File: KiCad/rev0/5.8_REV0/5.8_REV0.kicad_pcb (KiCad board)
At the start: 4 copper layers, 36 x 14.5 mm, 9 parts, among them J1 Conn_Coaxial, J2 Conn_01x02, U1 PMA3-83LN+

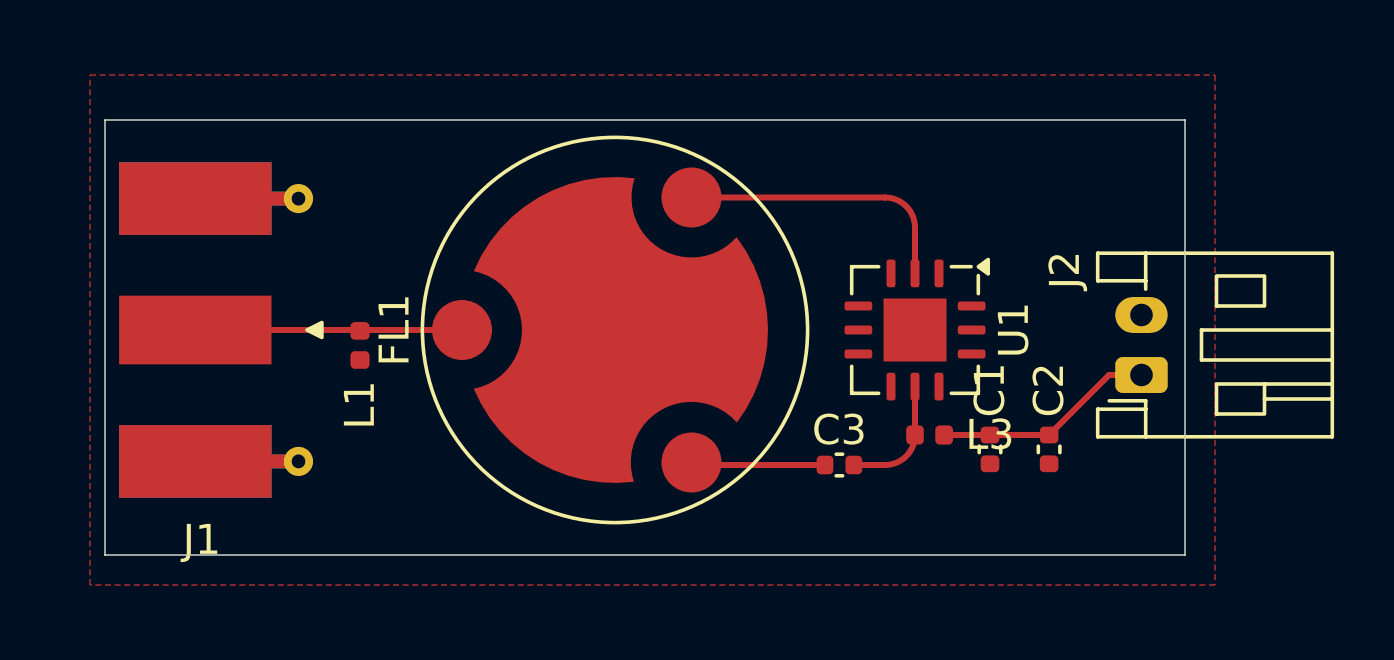
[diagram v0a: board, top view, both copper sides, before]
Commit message: Added sims and changed to microstrips
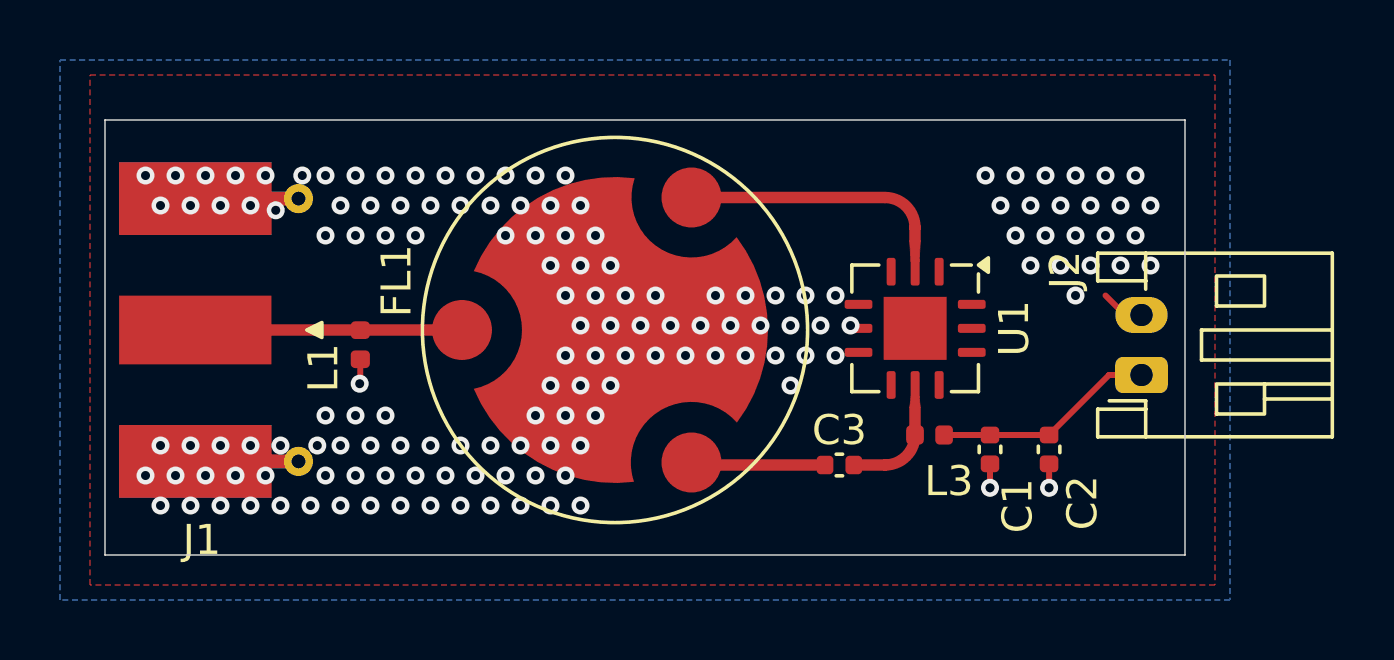
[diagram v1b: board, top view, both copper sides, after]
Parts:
- moved U1 0.06 mm to (155.5, 104.9)
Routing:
- net GND: track 0.00 -> 3.89 mm, vias 0 -> 149
- net Net-(FL1-P2): track 9.51 -> 8.40 mm
- net Net-(U1-RF_OUT_DC_IN): track 4.18 -> 3.43 mm
- added copper zone on B.Cu, net GND
- added copper zone on In1.Cu, net GND
- added copper zone on In2.Cu, net GND
